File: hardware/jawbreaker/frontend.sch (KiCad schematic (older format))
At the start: 113 parts, among them P1 TX-IN, P10 CONN_1, P11 CONN_1, P2 SERIAL, P3 RX-OUT, P4 ANTENNA, P5 CLK, P6 SWITCH_CTRL, P7 VCC, P8 CONN_1, P9 CONN_1, Q1 MOSFET_P, T1 MIX_IN_BALUN, T2 MIX_OUT_BALUN, U1 SKY13350, U10 SKY13350, U11 SKY13350, U12 SKY13317, U13 MGA-81563, U14 SKY13317, U15 GSG-74HC04, U16 GSG-74HC08, U2 SKY13350, U3 RX_LOWPASS_FILTER, U4 RFFC5072, U5 SKY13350, U6 SKY13350, U7 SKY13350, U8 RX_HIGHPASS_FILTER, U9 SKY13317

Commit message: re-annotated everything
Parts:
- renumbered C69 to C25, C25 to C26, C26 to C27, C27 to C28, C28 to C29, C29 to C30, C30 to C31, C31 to C32, C32 to C33, C33 to C34, C34 to C35, C35 to C36, C36 to C37, C37 to C38, C38 to C39, C39 to C40, C40 to C41, C41 to C42, C42 to C43, C43 to C44, C44 to C45, C45 to C46, C46 to C47, C47 to C48, C70 to C49, C48 to C50, C49 to C51, C50 to C52, C51 to C53, C52 to C54, C53 to C55, C55 to C56, C54 to C57, C56 to C58, C57 to C59, C58 to C60, C59 to C61, C60 to C62, C61 to C63, C62 to C64, C63 to C65, C64 to C66, C65 to C67, C66 to C68, C67 to C69, C68 to C70

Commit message: bom info, extra amp
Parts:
- removed P1: TX-IN, symbol GSG-SMA-CONN
- removed P10, P11, P8, P9: CONN_1, symbol CONN_1
- removed P3: RX-OUT, symbol GSG-SMA-CONN
- added C160: 100pF, symbol C
- added C161: 1uF, symbol C
- added C162, C163: 10nF, symbol C
- added L12: 1uH, symbol INDUCTOR
- added Q2: MOSFET_P, symbol MOSFET_P
- added R103: 33, symbol R
- added R? (x2): 4k7, symbol R
- added U25: MGA-81563, symbol MGA-81563
- L2, L3, L5: value 180nH -> 1uH; Description INDUCTOR 180NH .25A WW 0603 -> INDUCTR 1.0UH 650MA 20% 0603 SMD; Manufacturer Wurth -> Taiyo Yuden; Part Number 744761218C -> Digi-Key 587-2897-1-ND
- P2, P4, P5, P6, P7: Note (none) -> DNP
- T1, T2: Description (none) -> Ultra Low Profile 0805 Balun 50 to 100 ohm Balanced; Manufacturer (none) -> Anaren; Part Number (none) -> B0310J50100AHF
- U1, U10, U11, U2, U5, U6, U7: Description (none) -> 0.01-6.0 GHz GaAs SPDT Switch; Manufacturer (none) -> Skyworks; Part Number (none) -> SKY13350-385LF
- U12, U14, U9: Description (none) -> 20 MHz-6.0 GHz pHEMT GaAs SP3T Switch; Manufacturer (none) -> Skyworks; Part Number (none) -> SKY13317-373LF
- U13: Description (none) -> 0.1-6 GHz 3 V, 14 dBm Amplifier; Manufacturer (none) -> Avago; Part Number (none) -> MGA-81563
- U16: Description (none) -> IC QUAD 2IN POS-AND GATE 14-QFN; Manufacturer (none) -> Texas Instruments; Part Number (none) -> SN74AHC08RGYR
- U4: Description (none) -> WIDEBAND SYNTHESIZER/VCO WITH INTEGRATED 6GHz MIXER; Manufacturer (none) -> RFMD; Part Number (none) -> RFFC5072
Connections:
- net !AMP_PWR: now also R?.2
- net GND: now also C160.2, C161.2
- net VCC: now also R?.1
- net TX_IF: now reaches C8.1
- net RX_IF: now reaches C48.2
- new net: Q2.D, R103.1
- new net: C160.1, C161.1, L12.1, R103.2
- no-connect marks 9 -> 5
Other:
- note removed: "mounting holes"

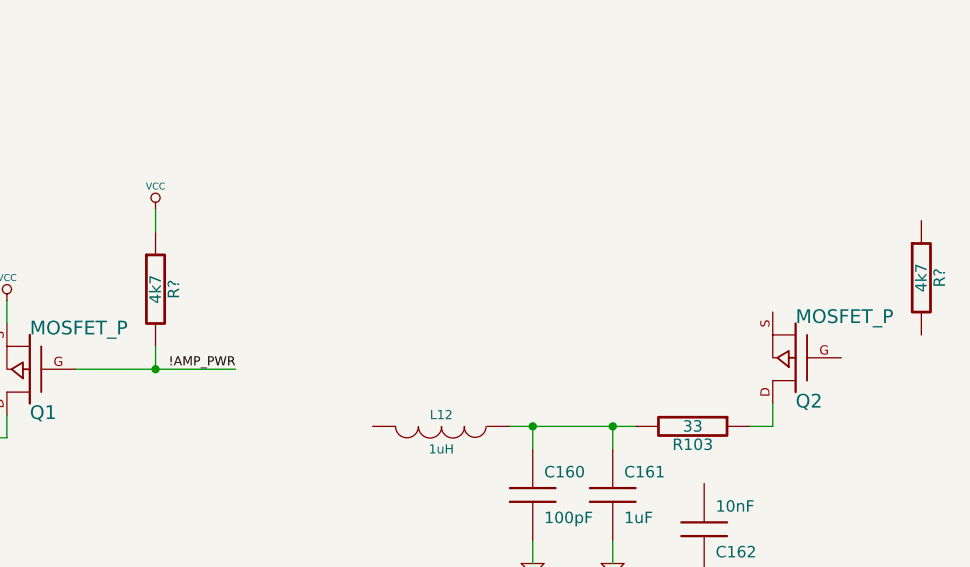
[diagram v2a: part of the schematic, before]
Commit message: started replacing 0603s with 0402s
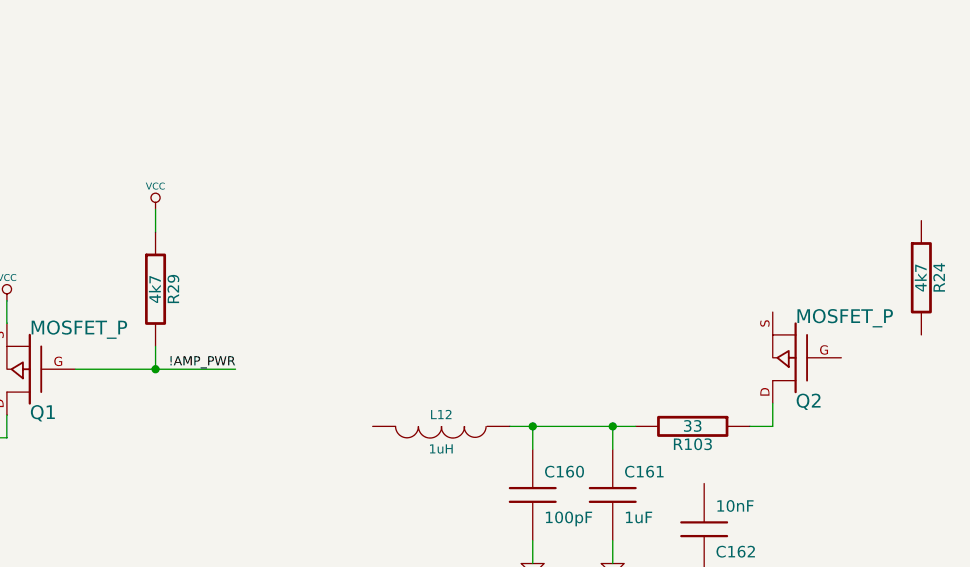
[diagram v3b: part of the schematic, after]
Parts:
- gave numbers to parts that had none: 2

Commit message: updated regulator feedback resistors
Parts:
- L12, L2, L3, L5: Part Number Digi-Key 587-2897-1-ND -> BRL1608T1R0M
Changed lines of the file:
@@
-EESchema Schematic File Version 2  date Mon Aug 27 23:13:08 2012
+EESchema Schematic File Version 2  date Thu Aug 30 09:18:56 2012
 LIBS:power
 LIBS:device
@@
 Sheet 2 4
 Title ""
-Date "28 aug 2012"
+Date "30 aug 2012"
 Rev ""
 Comp ""
@@
 F 1 "1uH" V 17650 6800 40  0000 C CNN
 F 4 "Taiyo Yuden" H 17550 6800 60  0001 C CNN "Manufacturer"
-F 5 "Digi-Key 587-2897-1-ND" H 17550 6800 60  0001 C CNN "Part Number"
+F 5 "BRL1608T1R0M" H 17550 6800 60  0001 C CNN "Part Number"
 F 6 "INDUCTR 1.0UH 650MA 20% 0603 SMD" H 17550 6800 60  0001 C CNN "Description"
 	1    17550 6800
@@
 F 1 "1uH" V 5150 5350 40  0000 C CNN
 F 4 "Taiyo Yuden" H 5050 5350 60  0001 C CNN "Manufacturer"
-F 5 "Digi-Key 587-2897-1-ND" H 5050 5350 60  0001 C CNN "Part Number"
+F 5 "BRL1608T1R0M" H 5050 5350 60  0001 C CNN "Part Number"
 F 6 "INDUCTR 1.0UH 650MA 20% 0603 SMD" H 5050 5350 60  0001 C CNN "Description"
 	1    5050 5350
@@
 F 1 "1uH" V 5150 5050 40  0000 C CNN
 F 4 "Taiyo Yuden" H 5050 5050 60  0001 C CNN "Manufacturer"
-F 5 "Digi-Key 587-2897-1-ND" H 5050 5050 60  0001 C CNN "Part Number"
+F 5 "BRL1608T1R0M" H 5050 5050 60  0001 C CNN "Part Number"
 F 6 "INDUCTR 1.0UH 650MA 20% 0603 SMD" H 5050 5050 60  0001 C CNN "Description"
 	1    5050 5050
@@
 F 1 "1uH" V 14300 6850 40  0000 C CNN
 F 4 "Taiyo Yuden" H 14200 6850 60  0001 C CNN "Manufacturer"
-F 5 "Digi-Key 587-2897-1-ND" H 14200 6850 60  0001 C CNN "Part Number"
+F 5 "BRL1608T1R0M" H 14200 6850 60  0001 C CNN "Part Number"
 F 6 "INDUCTR 1.0UH 650MA 20% 0603 SMD" H 14200 6850 60  0001 C CNN "Description"
 	1    14200 6850

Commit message: bom info
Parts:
- removed R103, R7: 33, symbol R
- C161, C53: Description (none) -> CAP CER 1UF 10V 20% X5R 0402; Manufacturer (none) -> Murata; Part Number (none) -> GRM155R61A105ME15D
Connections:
- net at C52.1, C53.1, L5.1: now also Q1.D
- net at Q2.D: now also C160.1, C161.1, L12.1

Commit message: optional RF LDO
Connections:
- net VCC: no longer C3.1, C4.1, C5.1, C6.1, Q1.S, R29.1, U4.22 (ANA_VDD2), U4.5 (ANA_VDD1)
- net at U1.4 (OUT2): no longer C32.1
- new net VAA: C3.1, C4.1, C5.1, C6.1, Q1.S, R29.1, U4.22 (ANA_VDD2), U4.5 (ANA_VDD1)
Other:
- moved on the sheet: C1, C2
